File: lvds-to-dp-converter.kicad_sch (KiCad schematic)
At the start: 40 parts, among them U25 TLV73318PDBVT, U27 IT6251, Y4 Resonator_27MHz_ABM7

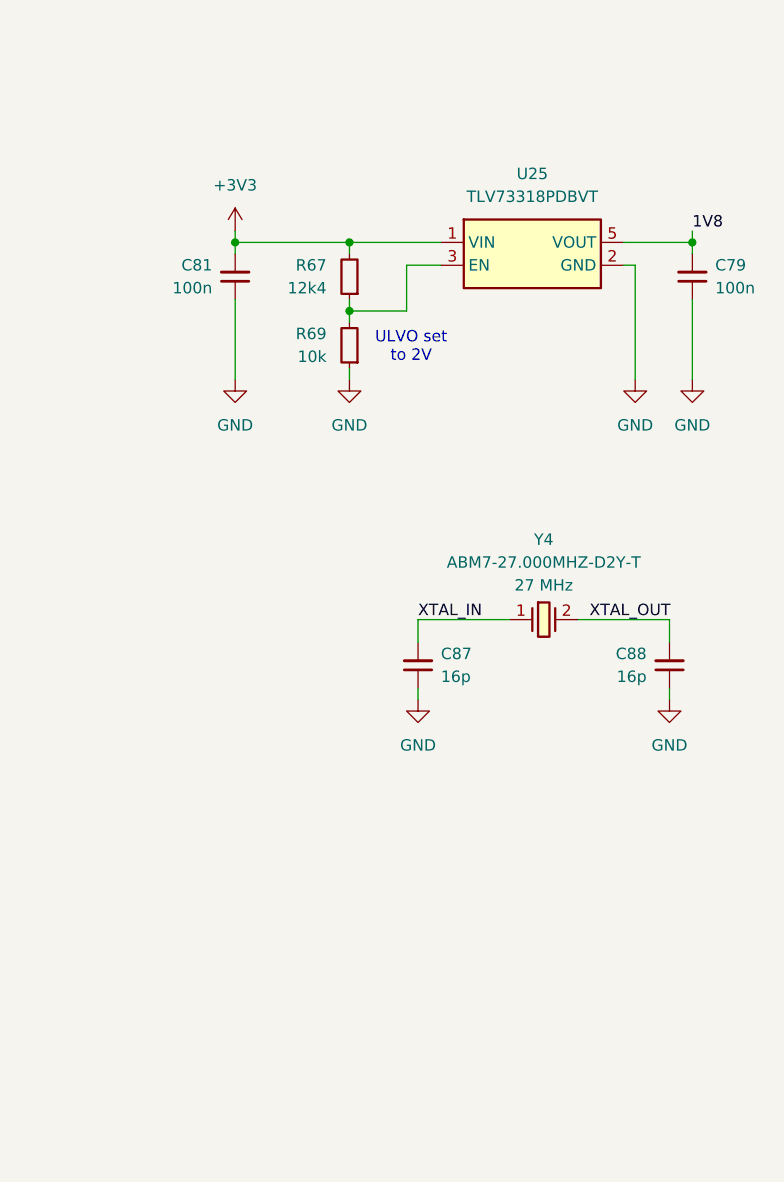
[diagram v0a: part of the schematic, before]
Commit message: [#82687] Use 500mA LDO
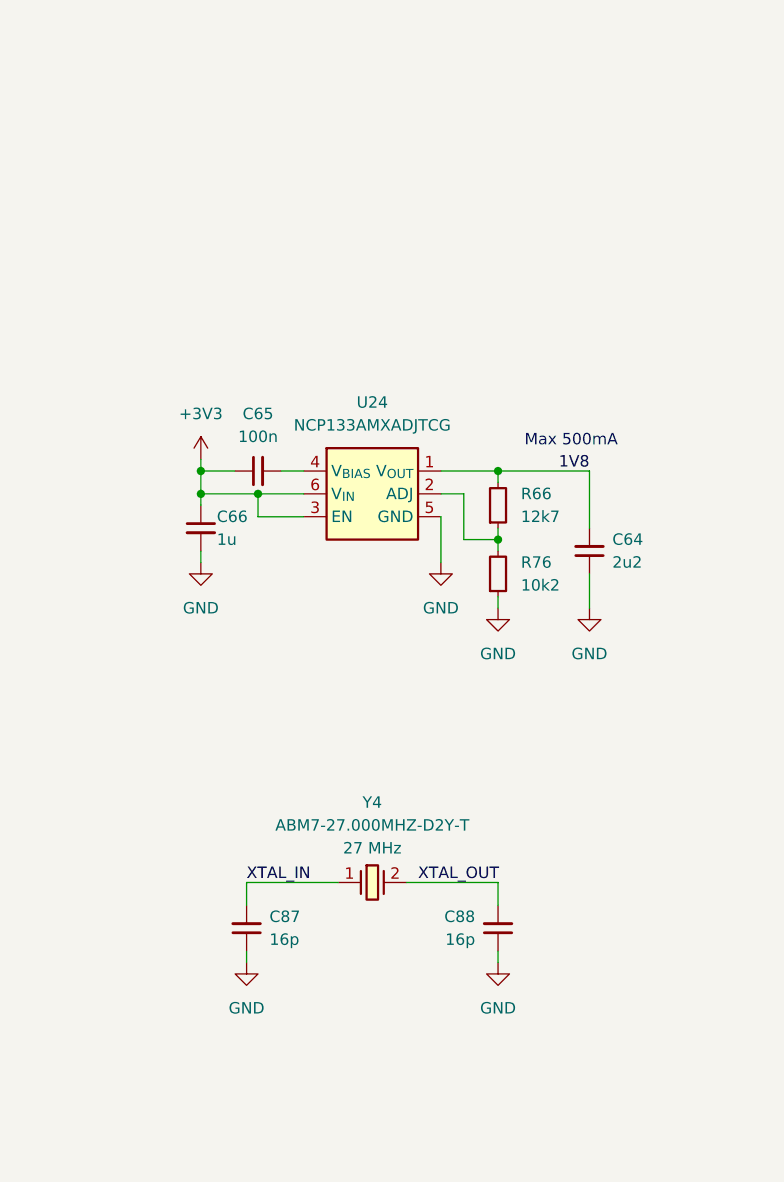
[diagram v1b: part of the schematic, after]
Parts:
- removed C79, C81: C_100n_0402, antmicro-footprints:C_0402_1005Metric, symbol antmicroCapacitors0402:C_100n_0402
- removed R67: R_12k4_0402, antmicro-footprints:R_0402_1005Metric, symbol antmicroResistors0402:R_12k4_0402
- removed R69: R_10k_0402, antmicro-footprints:R_0402_1005Metric, symbol antmicroResistors0402:R_10k_0402
- removed U25: TLV73318PDBVT, antmicro-footprints:SOT-23-5, symbol antmicroPMICVoltageRegulatorsLinear:TLV73318PDBVT
- added C64: C_2u2_0402, antmicro-footprints:C_0402_1005Metric, symbol antmicroCapacitors0402:C_2u2_0402
- added C65: C_100n_0402, antmicro-footprints:C_0402_1005Metric, symbol antmicroCapacitors0402:C_100n_0402
- added C66: C_1u_0402, antmicro-footprints:C_0402_1005Metric, symbol antmicroCapacitors0402:C_1u_0402
- added R66: R_12k7_0402, antmicro-footprints:R_0402_1005Metric, symbol antmicroResistors0402:R_12k7_0402
- added R76: R_10k2_0402, antmicro-footprints:R_0402_1005Metric, symbol antmicroResistors0402:R_10k2_0402
- added U24: NCP133AMXADJTCG, antmicro-footprints:XDFN-6_1.2x1.2mm_P0.4mm, symbol antmicroPMICVoltageRegulatorsLinear:NCP133AMXADJTCG
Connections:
- net +3V3: now also C65.1, C66.1, U24.3 (EN), U24.6 (V_{IN})
- net 1V8: now also C64.2, R66.2, U24.1 (V_{OUT})
- net GND: now also C64.1, C66.2, R76.1, U24.5 (GND), U24.EP (GND)
- new net: C65.2, U24.4 (V_{BIAS})
- new net: R66.1, R76.2, U24.2 (ADJ)
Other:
- note added: "Max 500mA"
- note removed: "ULVO set to 2V"
- moved on the sheet: C87, C88, Y4

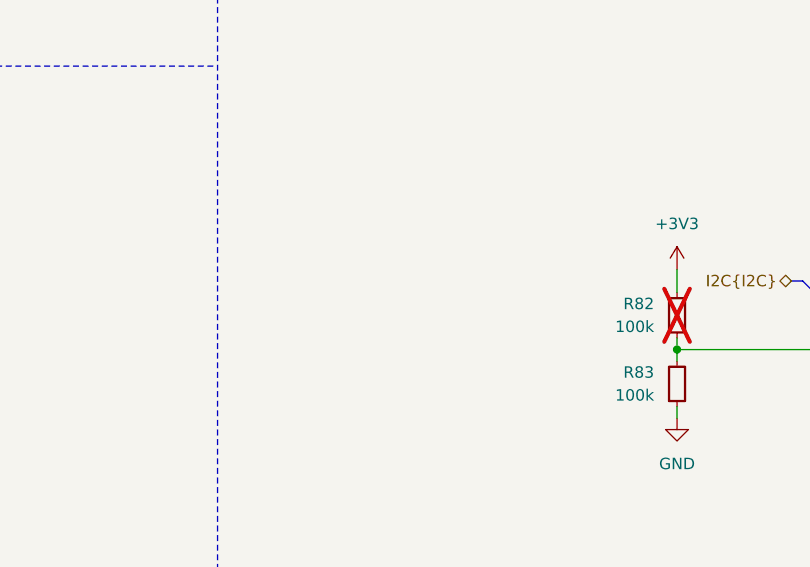
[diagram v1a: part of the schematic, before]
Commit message: [#82687] Update PCADR values
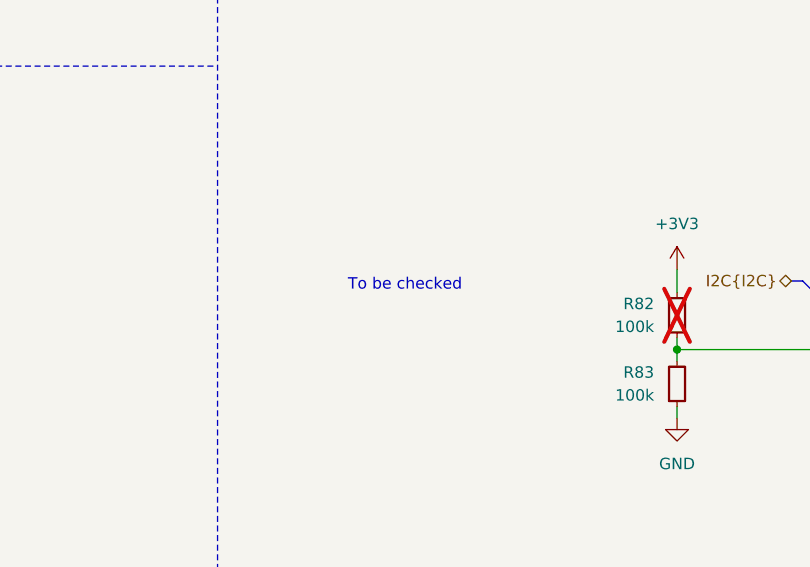
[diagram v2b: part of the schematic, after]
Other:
- note added: "To be checked"
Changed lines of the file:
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@@
+		)
+	)
+	(text "To be checked"
+		(exclude_from_sim no)
+		(at 138.684 114.808 0)
+		(effects
+			(font
+				(size 1.27 1.27)
+			)
 		)
 	)
@@
 			(table_cell "ADDR"
 				(exclude_from_sim no)
-				(at 139.7 117.602 0)
+				(at 132.08 116.84 0)
 				(size 8.89 2.54)
 				(margins 0.9525 0.9525 0.9525 0.9525)
@@
 			(table_cell "I2C ADDR"
 				(exclude_from_sim no)
-				(at 148.59 117.602 0)
+				(at 140.97 116.84 0)
 				(size 11.43 2.54)
 				(margins 0.9525 0.9525 0.9525 0.9525)
@@
 			(table_cell "LOW"
 				(exclude_from_sim no)
-				(at 139.7 120.142 0)
+				(at 132.08 119.38 0)
 				(size 8.89 2.54)
 				(margins 0.9525 0.9525 0.9525 0.9525)
@@
 				)
 			)
-			(table_cell "0x2C"
+			(table_cell "0x98"
 				(exclude_from_sim no)
-				(at 148.59 120.142 0)
+				(at 140.97 119.38 0)
 				(size 11.43 2.54)
 				(margins 0.9525 0.9525 0.9525 0.9525)
@@
 			(table_cell "HIGH"
 				(exclude_from_sim no)
-				(at 139.7 122.682 0)
+				(at 132.08 121.92 0)
 				(size 8.89 2.54)
 				(margins 0.9525 0.9525 0.9525 0.9525)
@@
 				)
 			)
-			(table_cell "0x2D"
+			(table_cell "0x9A"
 				(exclude_from_sim no)
-				(at 148.59 122.682 0)
+				(at 140.97 121.92 0)
 				(size 11.43 2.54)
 				(margins 0.9525 0.9525 0.9525 0.9525)

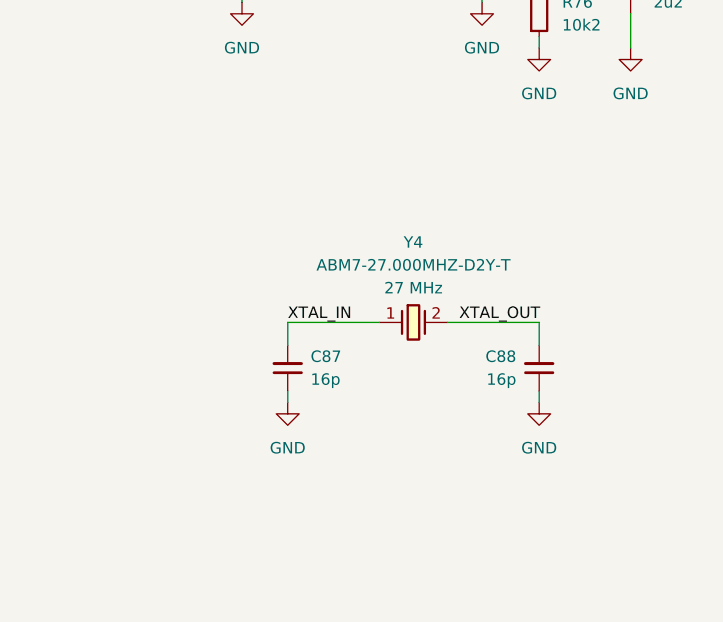
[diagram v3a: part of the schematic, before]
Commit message: [#83146] Fix LTPI connection, add bias
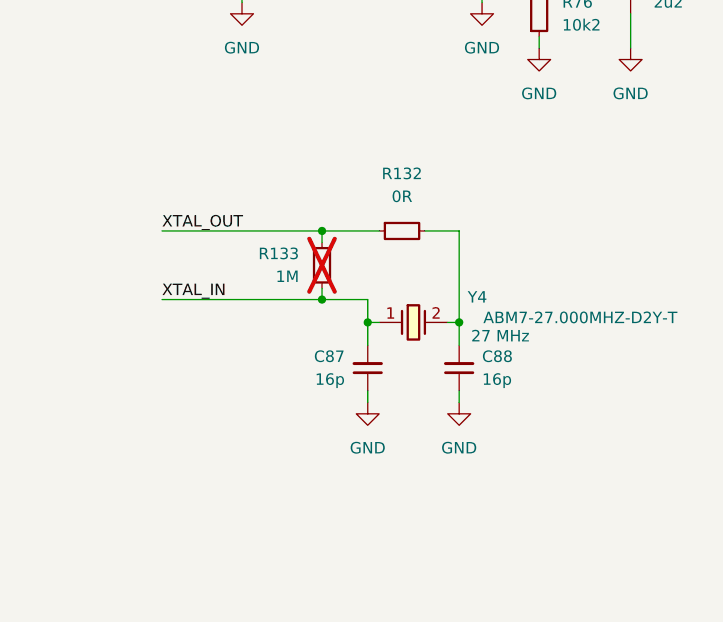
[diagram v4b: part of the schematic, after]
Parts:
- added R132: R_0R_0402, antmicro-footprints:R_0402_1005Metric, symbol antmicroResistors0402:R_0R_0402
- added R133: R_1M_0402, antmicro-footprints:R_0402_1005Metric, symbol antmicroResistors0402:R_1M_0402
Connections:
- net XTAL_IN: now also R133.1
- net XTAL_OUT: now also R132.1, R133.2; no longer C88.2, Y4.2
- new net: C88.2, R132.2, Y4.2
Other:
- moved on the sheet: C87, C88

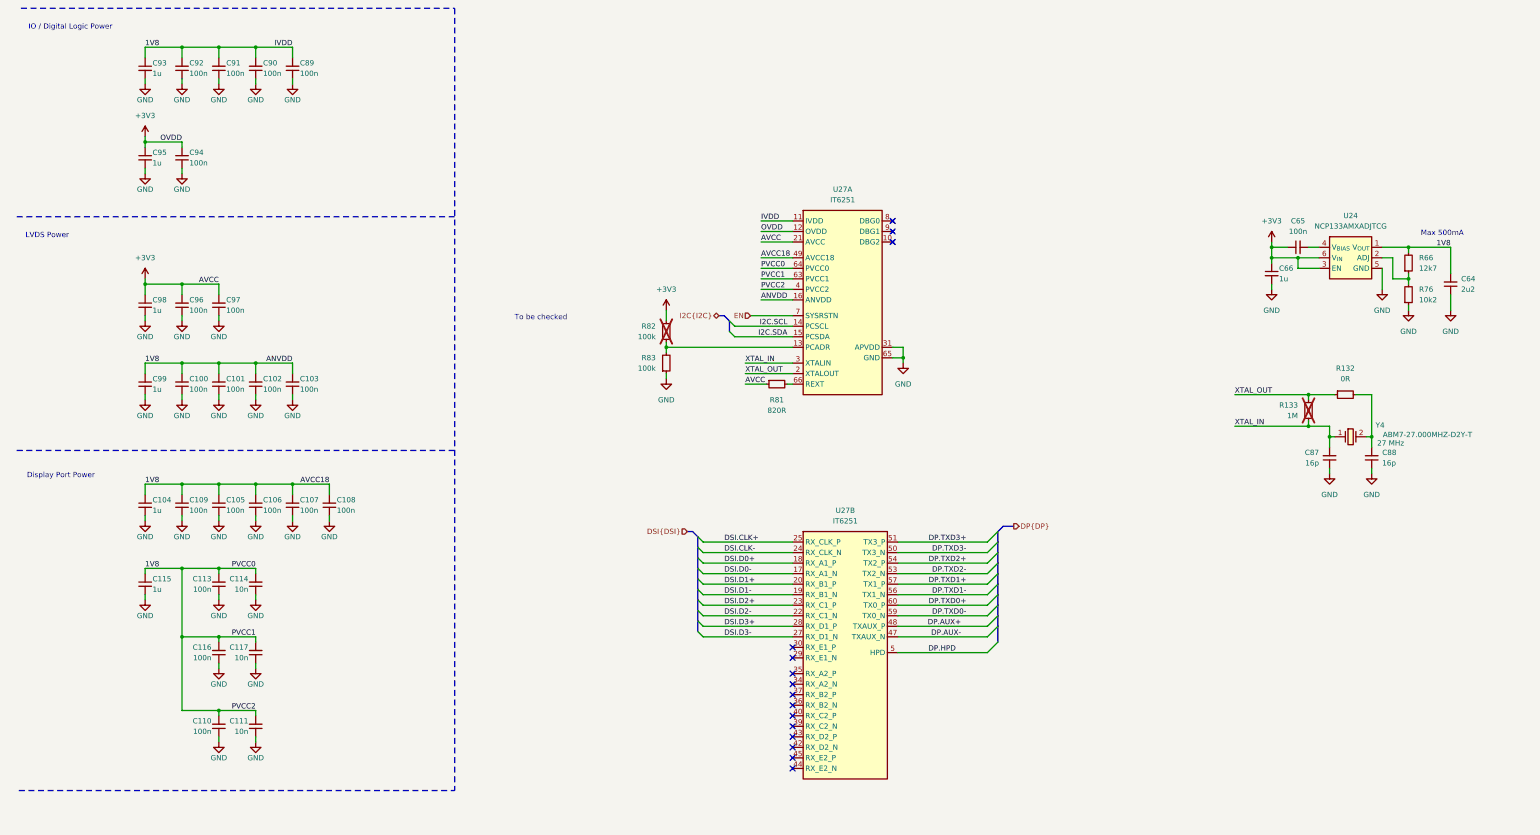
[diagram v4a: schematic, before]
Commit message: [#83363] Replaced 1V8 LDO with DC/DC and moved it to power sheet
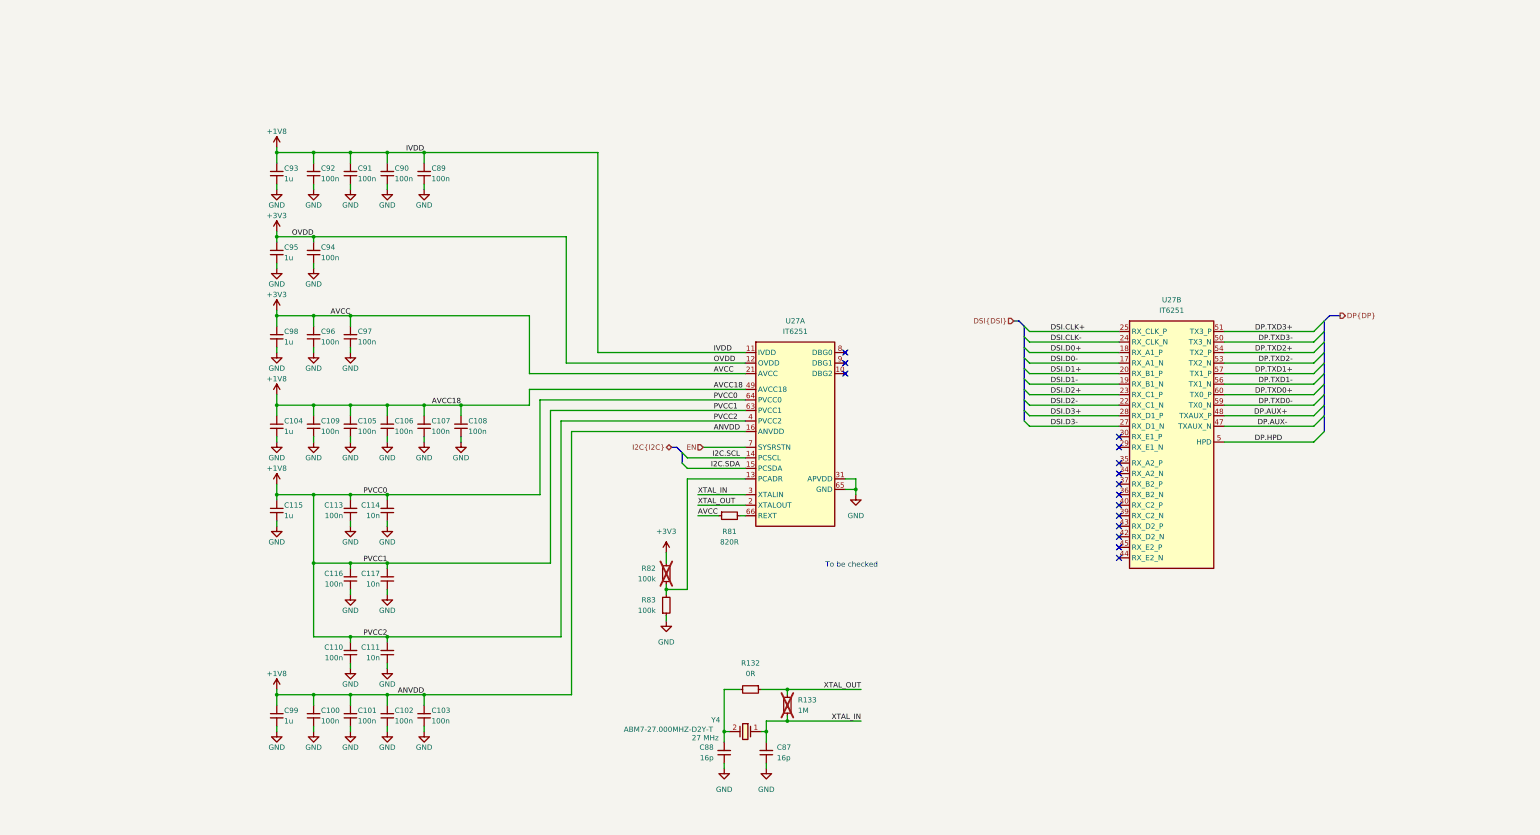
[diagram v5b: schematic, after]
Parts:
- removed C64: C_2u2_0402, antmicro-footprints:C_0402_1005Metric, symbol antmicroCapacitors0402:C_2u2_0402
- removed C65: C_100n_0402, antmicro-footprints:C_0402_1005Metric, symbol antmicroCapacitors0402:C_100n_0402
- removed C66: C_1u_0402, antmicro-footprints:C_0402_1005Metric, symbol antmicroCapacitors0402:C_1u_0402
- removed R66: R_12k7_0402, antmicro-footprints:R_0402_1005Metric, symbol antmicroResistors0402:R_12k7_0402
- removed R76: R_10k2_0402, antmicro-footprints:R_0402_1005Metric, symbol antmicroResistors0402:R_10k2_0402
- removed U24: NCP133AMXADJTCG, antmicro-footprints:XDFN-6_1.2x1.2mm_P0.4mm, symbol antmicroPMICVoltageRegulatorsLinear:NCP133AMXADJTCG
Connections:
- net 1V8 renamed +1V8
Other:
- note removed: "Display Port Power"
- note removed: "IO / Digital Logic Power"
- note removed: "LVDS Power"
- note removed: "Max 500mA"
- moved on the sheet: C100, C101, C102, C103, C104, C105, C106, C107, C108, C109, C110, C111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

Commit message: [#83363] Added LVDS termination
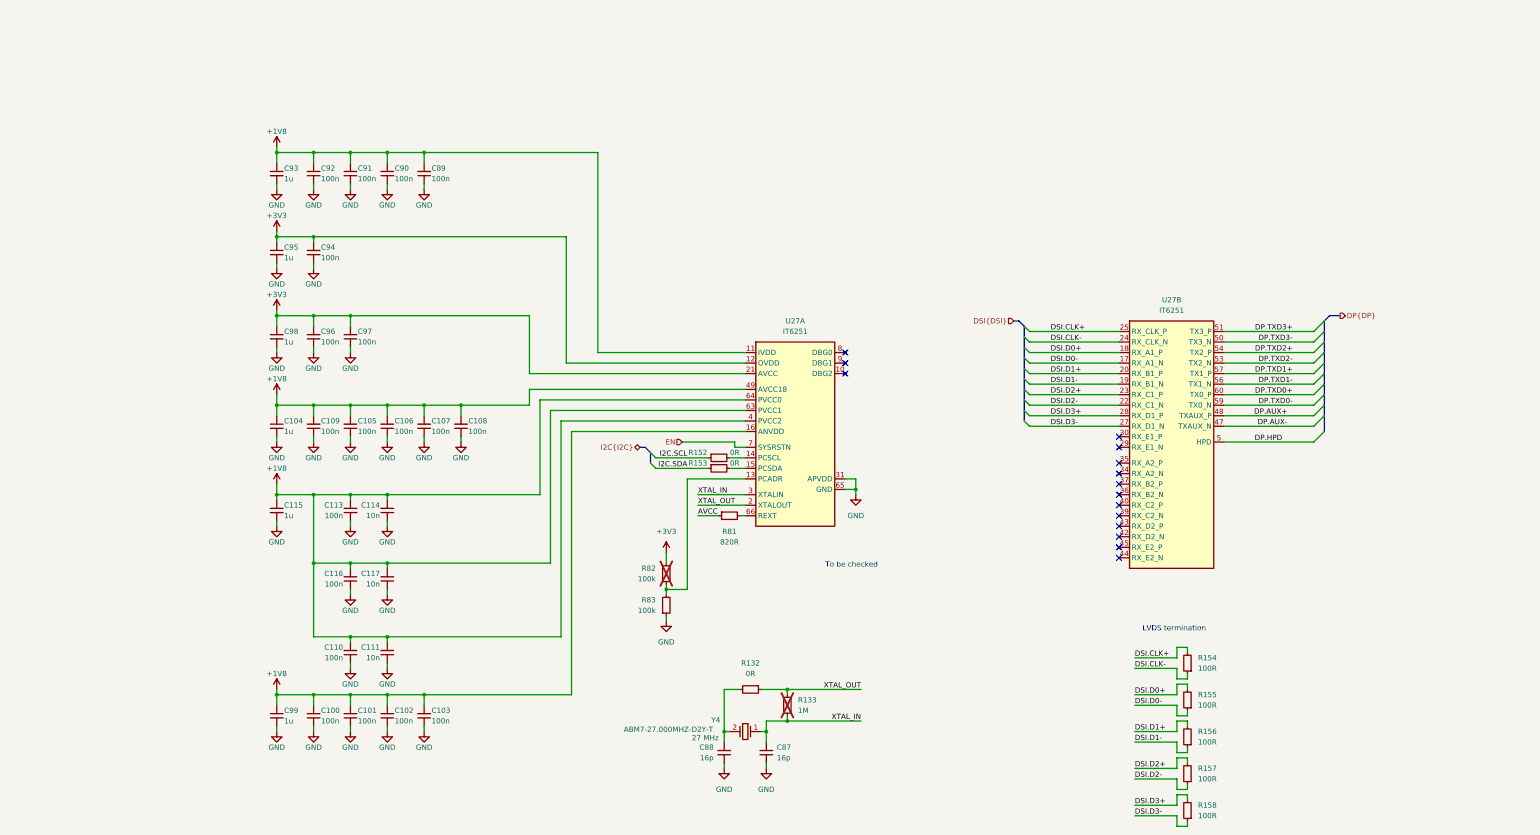
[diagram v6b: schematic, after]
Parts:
- added R152, R153: R_0R_0402, antmicro-footprints:R_0402_1005Metric, symbol antmicroResistors0402:R_0R_0402
- added R154, R155, R156, R157, R158: R_100R_0402, antmicro-footprints:R_0402_1005Metric, symbol antmicroResistors0402:R_100R_0402
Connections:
- net +3V3: no longer R81.1
- net DSI.CLK+: now also R154.2
- net DSI.CLK-: now also R154.1
- net DSI.D0+: now also R155.2
- net DSI.D0-: now also R155.1
- net DSI.D1+: now also R156.2
- net DSI.D1-: now also R156.1
- net DSI.D2+: now also R157.2
- net DSI.D2-: now also R157.1
- net DSI.D3+: now also R158.2
- net DSI.D3-: now also R158.1
- net I2C.SCL: now also R152.1; no longer U27.14 (PCSCL)
- net I2C.SDA: now also R153.1; no longer U27.15 (PCSDA)
- new net: R153.2, U27.15 (PCSDA)
- new net: R152.2, U27.14 (PCSCL)
- new net AVCC: R81.1
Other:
- note added: "LVDS termination"

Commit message: [#83609] Reannotate board
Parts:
- renumbered C92 to C100, C94 to C101, C96 to C102, C109 to C103, C100 to C104, C91 to C105, C97 to C106, C105 to C107, C113 to C108, C116 to C109, C101 to C111, C90 to C112, C106 to C113, C117 to C115, C111 to C116, C102 to C117, C89 to C118, C107 to C119, C103 to C120, C108 to C121, C88 to C122, C87 to C123, C93 to C94, C98 to C96, C104 to C97, C115 to C98, R82 to R202, R83 to R203, R152 to R204, R153 to R205, R81 to R206, R132 to R207, R133 to R208, R154 to R209, R155 to R210, R156 to R211, R157 to R212, R158 to R213, U27 to U24
